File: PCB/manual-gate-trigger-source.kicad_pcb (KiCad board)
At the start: 2 copper layers, 182.9 x 110.5 mm, 124 parts, among them J1 PWR, J10 IN1, J11 Conn_01x04, J12 Conn_01x04, J13 PWR_BRD, J14 INT_BRD, J2 OUTa, J3 OUTb, J4 OUTa, J5 OUTb, J6 OUTa, J7 OUTb, J8 OUTa, J9 OUTb, Q1 BC547, Q2 BC547, Q3 BC547, Q4 BC547, Q5 BC547, Q6 BC547, SW1 ON/OFF/ON, SW2 ON/ON, SW3 ON/ON, SW4 ON/ON, SW5 ON/ON, SW6 SW_Push, SW7 SW_Push, SW8 SW_Push, U1 TL072, U2 LM555xN, U3 LM555xN, U4 LM555xN, U5 LM555xN

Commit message: :art: State voltage range on adjustment pots
Use "lower", "middle", "upper" instead of actual values, as these might
be changed during assembly by chosing different resistors.
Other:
- board text added: "LOWER"
- board text added: "MIDDLE"
- board text added: "UPPER"

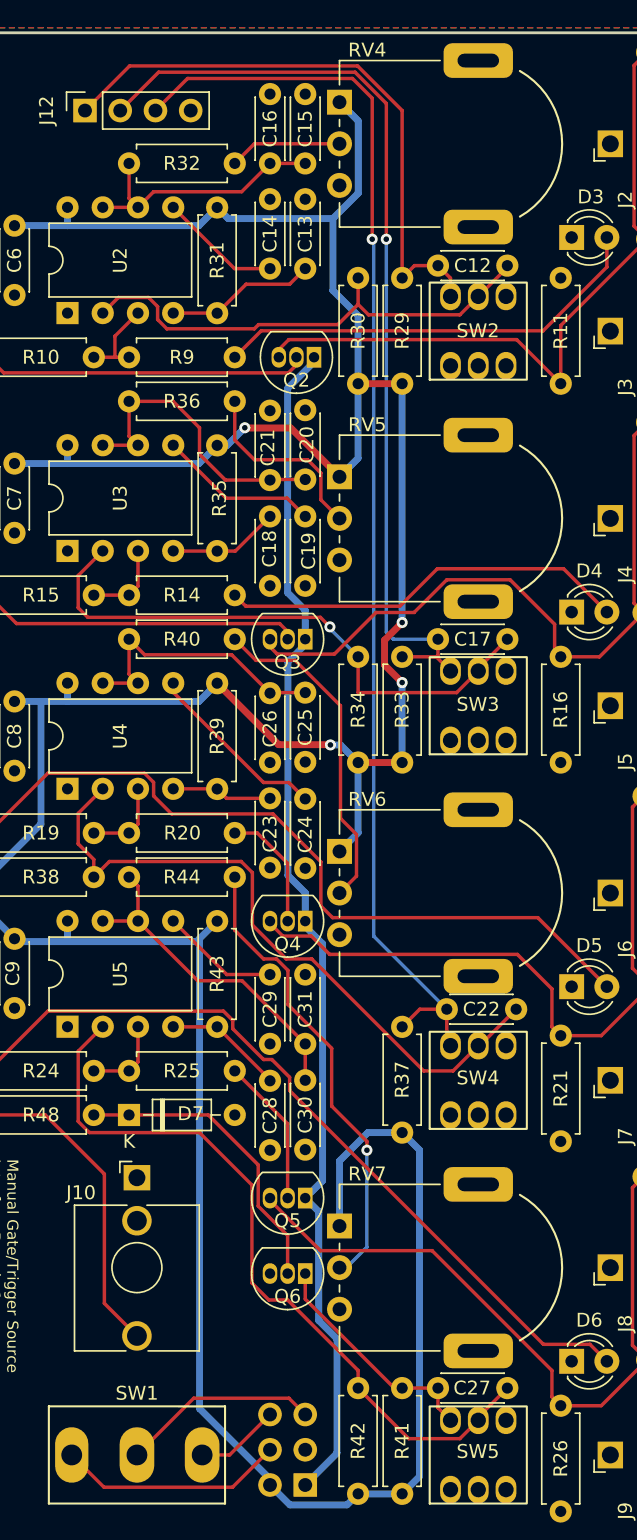
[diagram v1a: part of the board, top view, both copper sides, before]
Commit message: :pencil2: Adjust to fixed poti footprint
Adjust to fixed footprint from https://github.com/moPsy-project/moPsy-KiCad-resources/pull/14
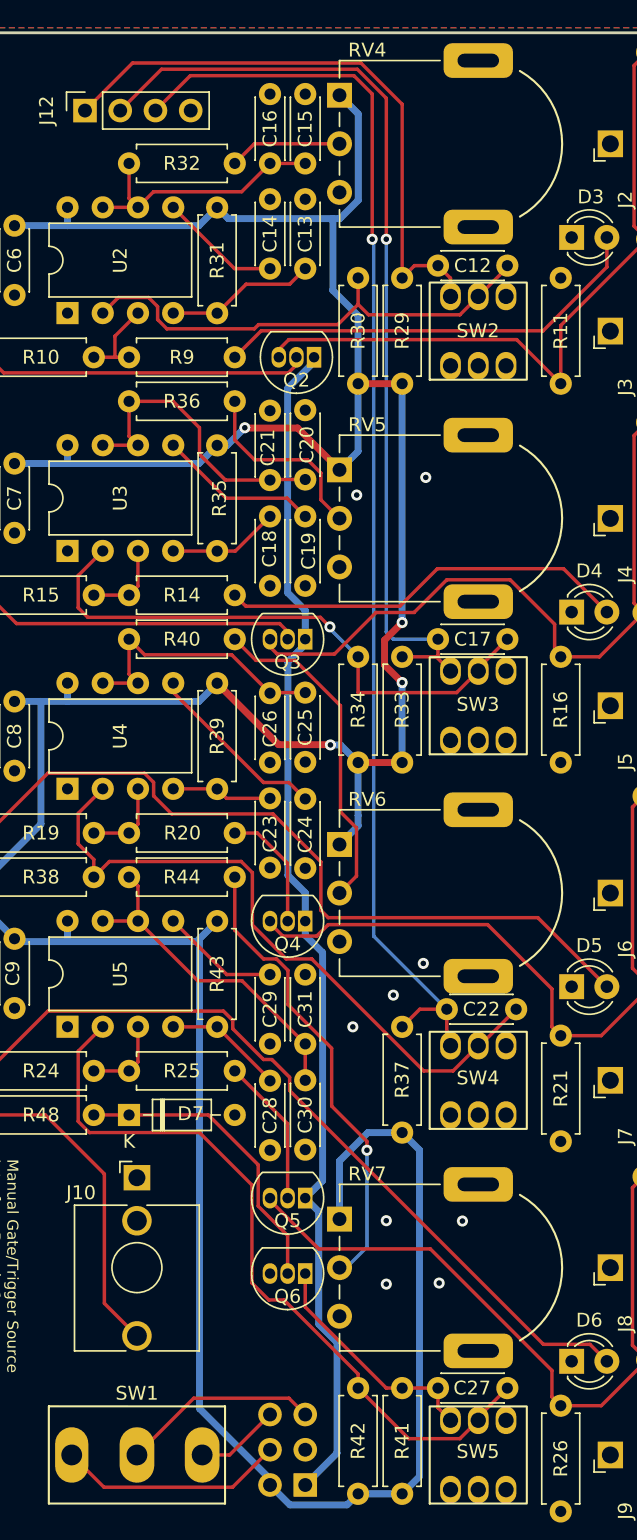
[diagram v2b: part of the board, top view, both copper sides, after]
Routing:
- net +12V: track 342.5 -> 341.6 mm
- net Net-(Q4-E): track 48.6 -> 49.3 mm
- net GND: vias 14 -> 23

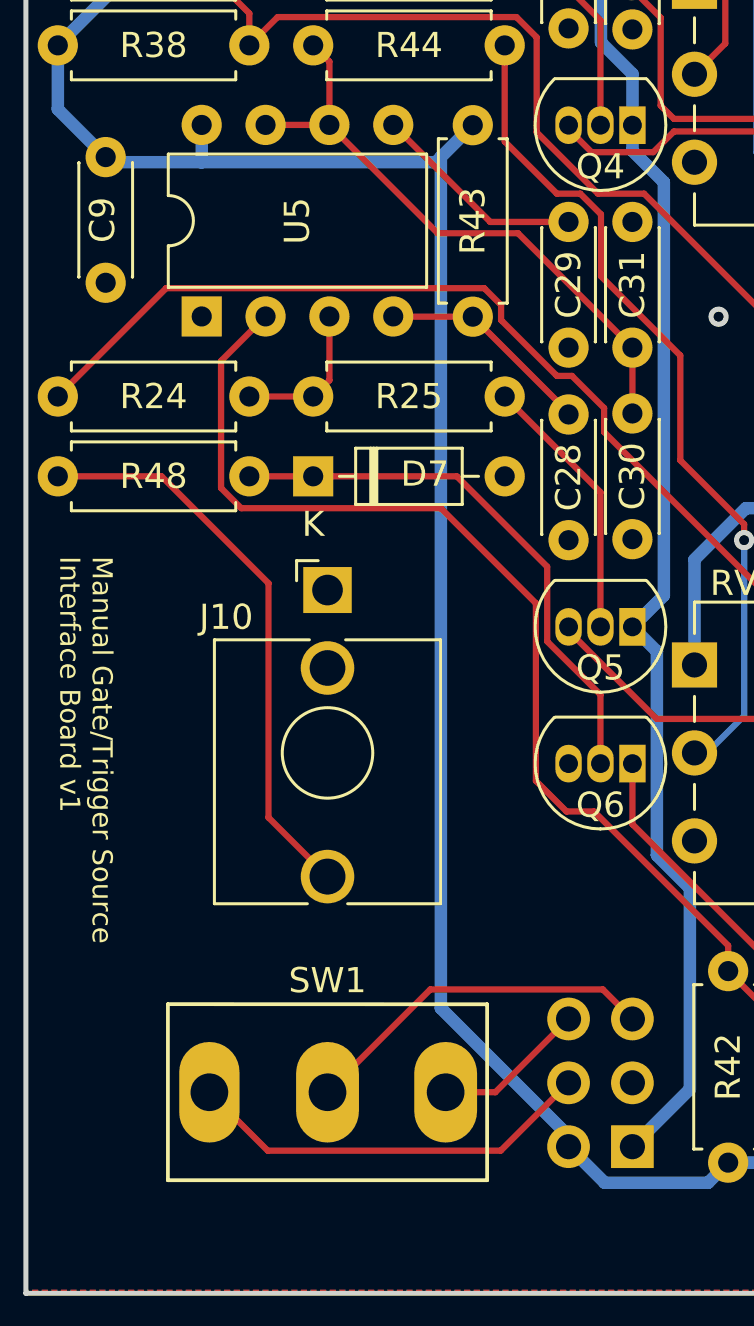
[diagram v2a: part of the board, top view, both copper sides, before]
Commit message: :hammer: Adjust PCB layout for changed footprint
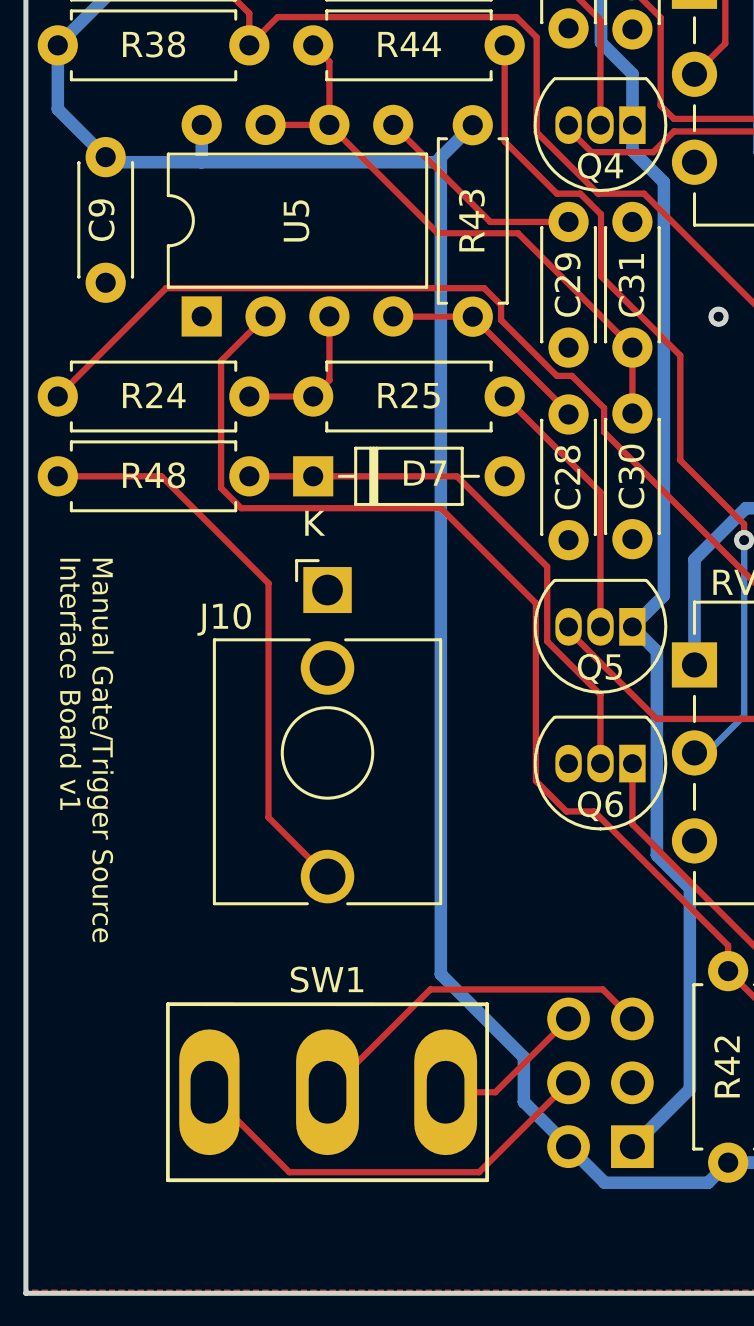
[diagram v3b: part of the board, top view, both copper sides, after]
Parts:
- SW1: footprint moPsy:Switch_SPDT_TSM103A2_Befaco -> moPsy:Switch_SPDT_TSM103A2_Befaco_flush
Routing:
- net Net-(J14-Pin_4): track 16.4 -> 17.1 mm
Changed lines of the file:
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@@
     )
   )
-  (footprint "moPsy:Switch_SPDT_TSM103A2_Befaco" locked (layer "F.Cu")
+  (footprint "moPsy:Switch_SPDT_TSM103A2_Befaco_flush" locked (layer "F.Cu")
     (at 110.5 143.5)
-    (descr "TSM103A2 Switch as sold by Befaco")
+    (descr "TSM103A2 Switch as sold by Befaco, flush fitting on the PCB")
     (property "Sheetfile" "manual-gate-trigger-source.kicad_sch")
     (property "Sheetname" "")
@@
     (fp_line (start 6.35 -3.5) (end 6.35 3.5)
       (stroke (width 0.15) (type solid)) (layer "F.SilkS"))
-    (pad "1" thru_hole oval locked (at -4.7 0) (size 2.4 4) (drill 1.5) (layers "*.Cu" "*.Mask")
+    (pad "1" thru_hole oval locked (at -4.7 0) (size 2.4 5) (drill oval 1.5 2.5) (layers "*.Cu" "*.Mask")
       (net 80 "Net-(J14-Pin_4)") (pinfunction "A") (pintype "passive"))
-    (pad "2" thru_hole oval locked (at 0 0) (size 2.5 4) (drill 1.5) (layers "*.Cu" "*.Mask")
+    (pad "2" thru_hole oval locked (at 0 0) (size 2.5 5) (drill oval 1.5 2.5) (layers "*.Cu" "*.Mask")
       (net 81 "Net-(J14-Pin_5)") (pinfunction "B") (pintype "passive"))
-    (pad "3" thru_hole oval locked (at 4.7 0) (size 2.5 4) (drill 1.5) (layers "*.Cu" "*.Mask")
+    (pad "3" thru_hole oval locked (at 4.7 0) (size 2.5 5) (drill oval 1.5 2.5) (layers "*.Cu" "*.Mask")
       (net 82 "Net-(J14-Pin_6)") (pinfunction "C") (pintype "passive"))
   )
@@
   (segment (start 105.495 89.18) (end 105.485 89.19) (width 0.5) (layer "B.Cu") (net 3))
   (segment (start 116.28 70.735) (end 114.97 72.045) (width 0.5) (layer "B.Cu") (net 3))
+  (segment (start 115.01 138.807) (end 118.312 142.109) (width 0.5) (layer "B.Cu") (net 3))
   (segment (start 126.44 66.29) (end 126.44 61.387233) (width 0.5) (layer "B.Cu") (net 3))
   (segment (start 114.97 72.045) (end 105.485 72.045) (width 0.5) (layer "B.Cu") (net 3))
-  (segment (start 120.09 145.235837) (end 120.09 145.665) (width 0.5) (layer "B.Cu") (net 3))
   (segment (start 114.97 54.9) (end 116.28 53.59) (width 0.5) (layer "B.Cu") (net 3))
   (segment (start 101.879999 106.499999) (end 114.805001 106.499999) (width 0.5) (layer "B.Cu") (net 3))
@@
   (segment (start 115.01 106.295) (end 116.28 105.025) (width 0.5) (layer "B.Cu") (net 3))
   (segment (start 116.28 53.59) (end 117.079999 54.389999) (width 0.5) (layer "B.Cu") (net 3))
+  (segment (start 118.312 143.887) (end 120.09 145.665) (width 0.5) (layer "B.Cu") (net 3))
   (segment (start 103.58 89.19) (end 105.485 89.19) (width 0.5) (layer "B.Cu") (net 3))
+  (segment (start 115.01 106.295) (end 115.01 138.807) (width 0.5) (layer "B.Cu") (net 3))
   (segment (start 105.485 72.045) (end 101.675 72.045) (width 0.5) (layer "B.Cu") (net 3))
+  (segment (start 118.312 142.109) (end 118.312 143.887) (width 0.5) (layer "B.Cu") (net 3))
   (segment (start 125.640001 147.099999) (end 121.524999 147.099999) (width 0.5) (layer "B.Cu") (net 3))
   (segment (start 126.45 46.85) (end 125.1 45.5) (width 0.5) (layer "B.Cu") (net 3))
@@
   (segment (start 99.77 101.85) (end 99.77 104.39) (width 0.5) (layer "B.Cu") (net 3))
   (segment (start 129.615 120.265) (end 130.865 121.515) (width 0.5) (layer "B.Cu") (net 3))
-  (segment (start 115.01 140.155837) (end 120.09 145.235837) (width 0.5) (layer "B.Cu") (net 3))
-  (segment (start 115.01 106.295) (end 115.01 140.155837) (width 0.5) (layer "B.Cu") (net 3))
   (segment (start 126.44 93.595) (end 126.44 97.405) (width 0.5) (layer "B.Cu") (net 3))
   (segment (start 125.1 72.5) (end 126.44 71.16) (width 0.5) (layer "B.Cu") (net 3))
@@
   (segment (start 217.084009 140.585) (end 219.27 140.585) (width 0.25) (layer "F.Cu") (net 79))
   (segment (start 219.27 140.585) (end 221.215 142.53) (width 0.25) (layer "F.Cu") (net 79))
-  (segment (start 117.39 145.825) (end 120.09 143.125) (width 0.25) (layer "F.Cu") (net 80))
-  (segment (start 105.8 143.5) (end 108.125 145.825) (width 0.25) (layer "F.Cu") (net 80))
-  (segment (start 108.125 145.825) (end 117.39 145.825) (width 0.25) (layer "F.Cu") (net 80))
+  (segment (start 116.534 146.681) (end 120.09 143.125) (width 0.25) (layer "F.Cu") (net 80))
+  (segment (start 108.981 146.681) (end 116.534 146.681) (width 0.25) (layer "F.Cu") (net 80))
+  (segment (start 105.8 143.5) (end 108.981 146.681) (width 0.25) (layer "F.Cu") (net 80))
   (segment (start 114.59 139.41) (end 121.455 139.41) (width 0.25) (layer "F.Cu") (net 81))
   (segment (start 110.5 143.5) (end 114.59 139.41) (width 0.25) (layer "F.Cu") (net 81))

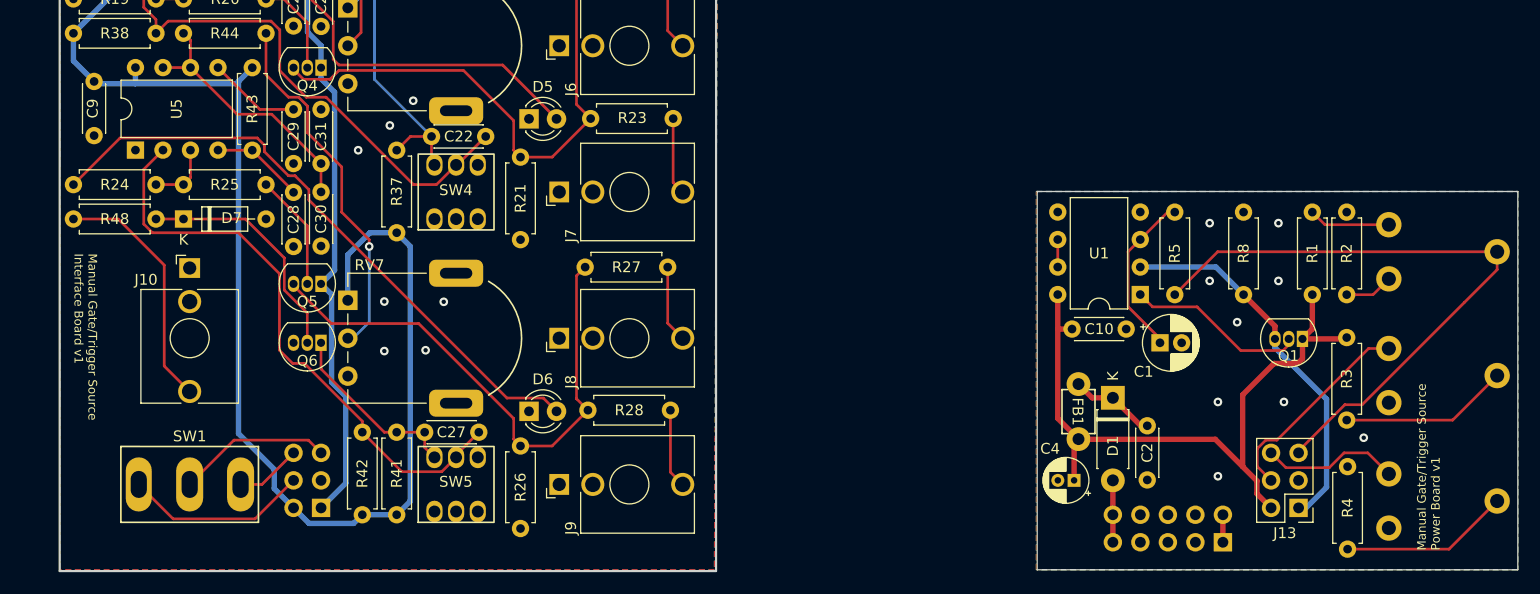
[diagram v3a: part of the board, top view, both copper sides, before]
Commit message: :hammer: Change PCB layout to match new schematic
This also fixes #46
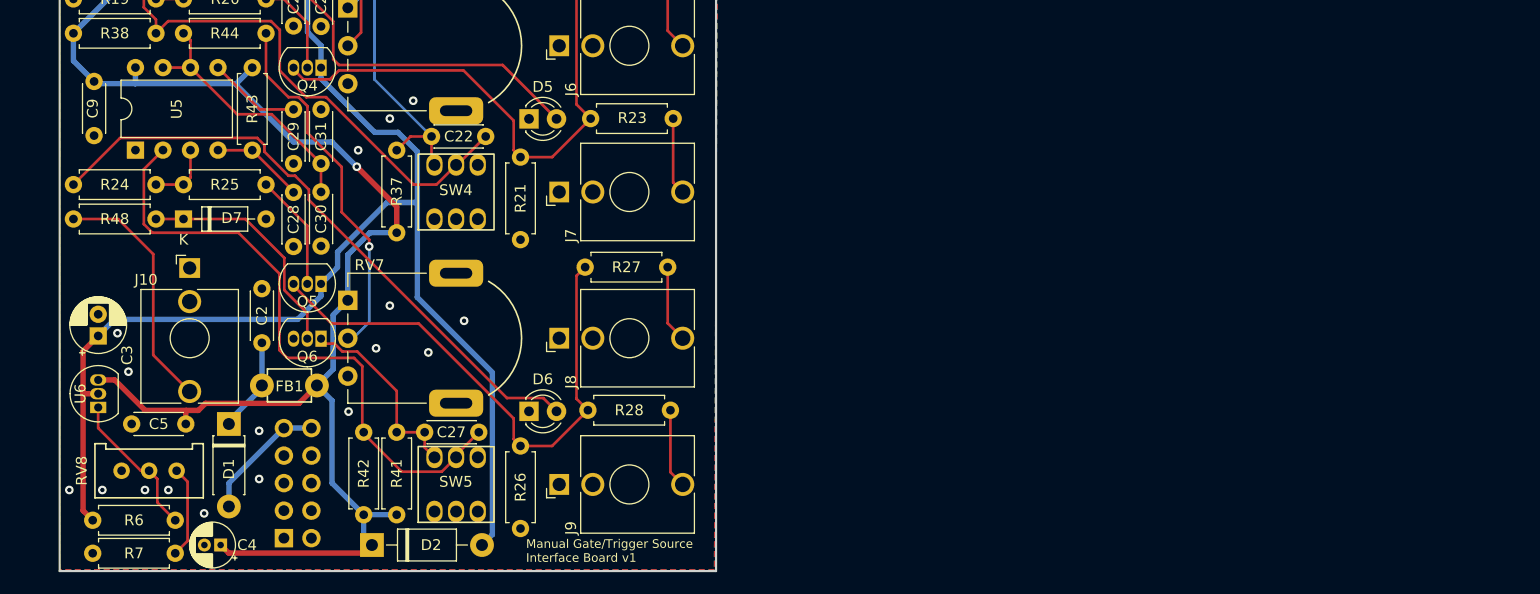
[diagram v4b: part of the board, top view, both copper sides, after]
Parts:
- removed C1: 1u, Capacitor_THT:CP_Radial_D5.0mm_P2.00mm
- removed C10: 100n, Capacitor_THT:C_Disc_D4.3mm_W1.9mm_P5.00mm
- removed J13: PWR_BRD, Connector_PinHeader_2.54mm:PinHeader_2x03_P2.54mm_Vertical
- removed J14: INT_BRD, Connector_PinSocket_2.54mm:PinSocket_2x03_P2.54mm_Vertical
- removed Q1: BC547, Package_TO_SOT_THT:TO-92_Inline
- removed R1: 71k5, Resistor_THT:R_Axial_DIN0207_L6.3mm_D2.5mm_P7.62mm_Horizontal
- removed R2: 49k9, Resistor_THT:R_Axial_DIN0207_L6.3mm_D2.5mm_P7.62mm_Horizontal
- removed R3: 39k, Resistor_THT:R_Axial_DIN0207_L6.3mm_D2.5mm_P7.62mm_Horizontal
- removed R4: 44k2, Resistor_THT:R_Axial_DIN0207_L6.3mm_D2.5mm_P7.62mm_Horizontal
- removed R5, R8: 10k, Resistor_THT:R_Axial_DIN0207_L6.3mm_D2.5mm_P7.62mm_Horizontal
- removed RV1, RV2, RV3: 10k, Potentiometer_THT:Potentiometer_Piher_PT-10-V10_Vertical
- removed SW1: ON/OFF/ON, moPsy:Switch_SPDT_TSM103A2_Befaco_flush
- removed U1: TL072, Package_DIP:DIP-8_W7.62mm
- added C3: 1u, Capacitor_THT:CP_Radial_D5.0mm_P2.00mm, F.Cu at (102.1, 129.8)
- added C5: 100n, Capacitor_THT:C_Disc_D4.3mm_W1.9mm_P5.00mm, F.Cu at (110.1, 137.9)
- added D2: 1N4002, Diode_THT:D_DO-41_SOD81_P10.16mm_Horizontal, F.Cu at (127.3, 149.1)
- added R6: 330R, Resistor_THT:R_Axial_DIN0207_L6.3mm_D2.5mm_P7.62mm_Horizontal, F.Cu at (101.5, 146.8)
- added R7: 470R, Resistor_THT:R_Axial_DIN0207_L6.3mm_D2.5mm_P7.62mm_Horizontal, F.Cu at (109.2, 149.9)
- added RV8: 2k, moPsy:Suntan 3296 Trim Pot, F.Cu at (106.8, 142.2)
- added U6: LM317L_TO92, Package_TO_SOT_THT:TO-92_Inline, F.Cu at (102.1, 136.4)
- moved J1 86.7 mm to (119.2, 148.5), turned to 0 degrees
- moved C2 82.1 mm to (117.2, 130.4), turned to 90 degrees
- moved D1 81.6 mm to (114.1, 137.9)
- moved C4 79.0 mm to (113.4, 149.1)
- moved FB1 72.9 mm to (119.7, 134.4), turned to 0 degrees
- moved Q6 0.38 mm to (122.6, 130.0)
- moved R42 0.13 mm to (126.6, 138.7)
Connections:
- J1 pad 1: /-12V_IN -> unconnected-(J1-Pin_1-Pad1)
- J1 pad 2: /-12V_IN -> unconnected-(J1-Pin_2-Pad2)
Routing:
- net TVS2: track 58.5 -> 0.00 mm
- net +12V: track 341.6 -> 287.2 mm, vias 4 -> 5
- net Vdrive: track 121.5 -> 150.7 mm
- net TVS1: track 19.4 -> 0.00 mm
- net Net-(J14-Pin_4): track 17.1 -> 0.00 mm
- net Net-(Q1-B): track 16.6 -> 0.00 mm
- net Net-(R4-Pad1): track 15.7 -> 0.00 mm
- net Net-(R3-Pad2): track 15.6 -> 0.00 mm
- net Net-(U1A-+): track 15.5 -> 0.00 mm
- net Net-(J14-Pin_5): track 14.3 -> 0.00 mm
- net Net-(U6-ADJ): track 0.00 -> 13.8 mm
- net TVS3: track 12.8 -> 0.00 mm
- net Net-(R7-Pad1): track 0.00 -> 8.51 mm
- net Net-(R1-Pad2): track 7.55 -> 0.00 mm
- net /+12V_IN: track 5.72 -> 11.9 mm
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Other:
- board size 182.9 x 110.5 mm -> 108.9 x 110.5 mm
- board text removed: "LOWER"
- board text removed: "MIDDLE"
- board text removed: "Manual Gate/Trigger Source Power Board v1"
- board text removed: "UPPER"
